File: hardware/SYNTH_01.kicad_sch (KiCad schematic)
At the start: 55 parts, among them J2 Conn_01x04_Pin, SW1 SW_Push_45deg, SW10 SW_Push_45deg, SW11 SW_Push_45deg, SW12 SW_Push_45deg, SW13 SW_Push_45deg, SW14 SW_Push_45deg, SW15 SW_Push_45deg, SW16 SW_Push_45deg, SW17 SW_Push_45deg, SW18 SW_Push_45deg, SW19 SW_Push_45deg, SW2 SW_Push_45deg, SW20 SW_Push_45deg, SW21 SW_Push_45deg, SW3 SW_Push_45deg, SW4 SW_Push_45deg, SW5 SW_Push_45deg, SW6 SW_Push_45deg, SW7 SW_Push_45deg, SW8 SW_Push_45deg, SW9 SW_Push_45deg, U1 MCP23017-E/SP

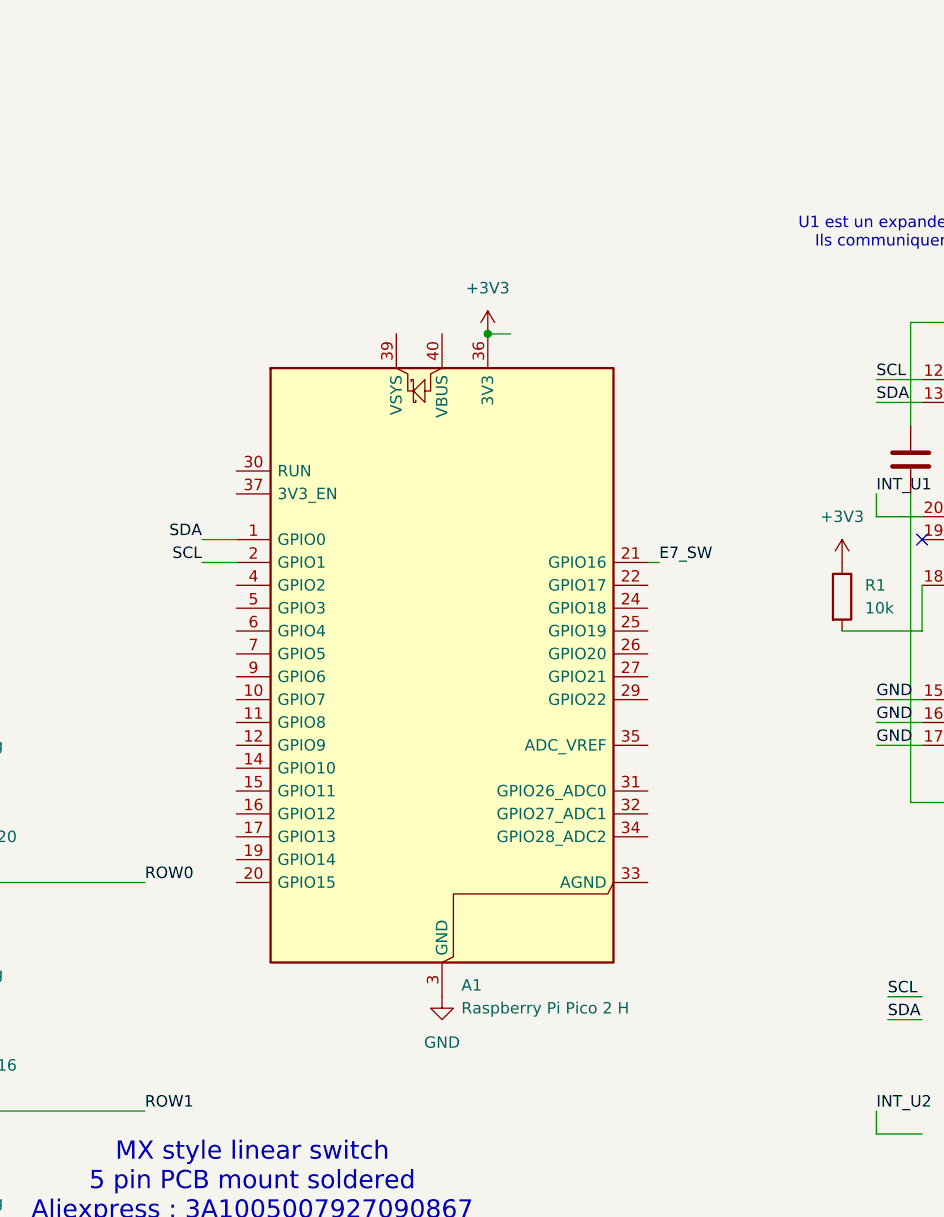
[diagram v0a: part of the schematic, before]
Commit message: PCB: rotary connexion to pico 2
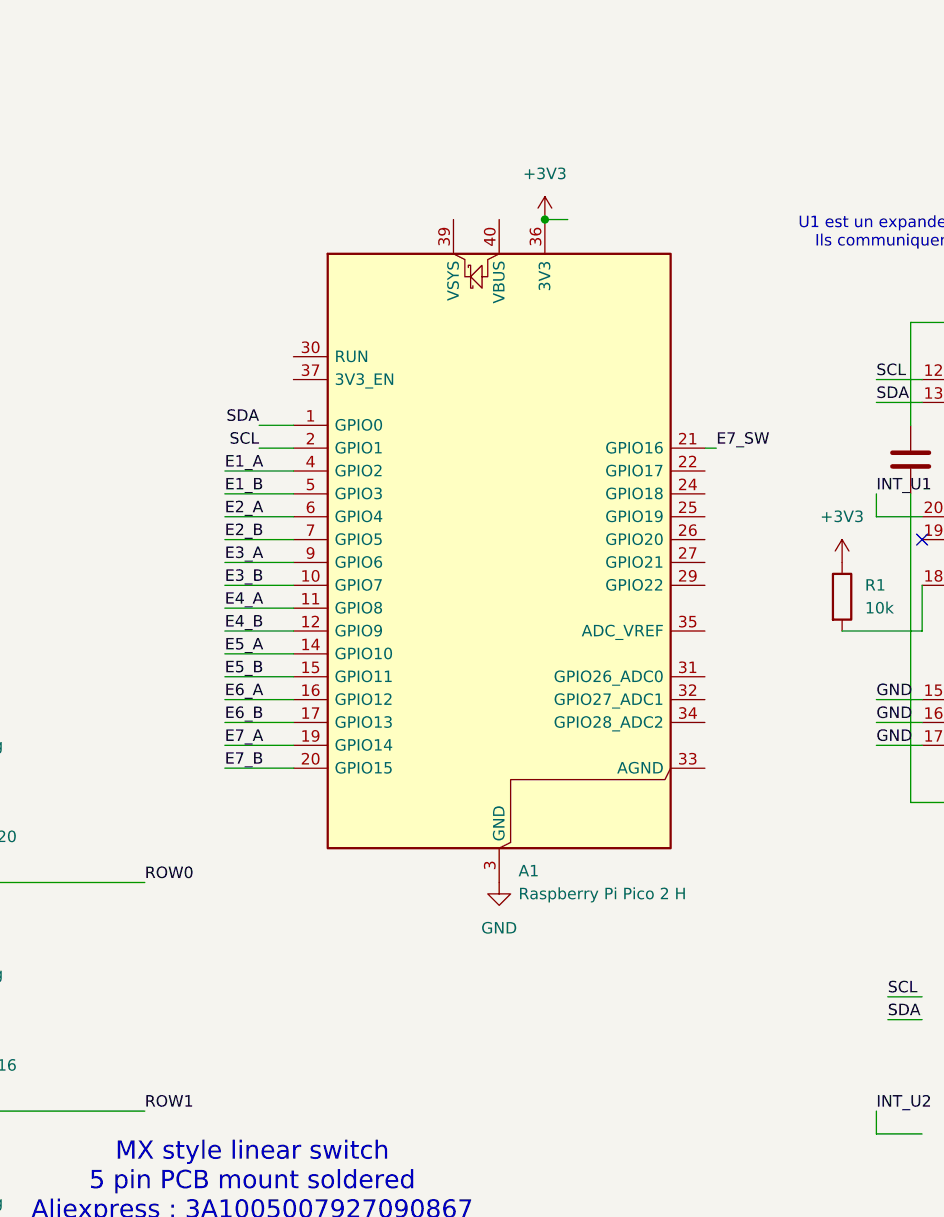
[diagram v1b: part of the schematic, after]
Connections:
- net E1_A: now also A1.4 (GPIO2)
- net E1_B: now also A1.5 (GPIO3)
- net E2_A: now also A1.6 (GPIO4)
- net E2_B: now also A1.7 (GPIO5)
- net E3_A: now also A1.9 (GPIO6)
- net E3_B: now also A1.10 (GPIO7)
- net E4_A: now also A1.11 (GPIO8)
- net E4_B: now also A1.12 (GPIO9)
- net E5_A: now also A1.14 (GPIO10)
- net E5_B: now also A1.15 (GPIO11)
- net E6_A: now also A1.16 (GPIO12)
- net E6_B: now also A1.17 (GPIO13)
- net E7_A: now also A1.19 (GPIO14)
- net E7_B: now also A1.20 (GPIO15)
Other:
- moved on the sheet: A1

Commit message: PCB: adding no connexion markers
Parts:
- D1, D10, D11, D12, D13, D14, D15, D16, D17, D18, D19, D2, D20, D3, D4, D5, D6, D7, D8, D9: value D -> 1N4148
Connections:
- net INT_U1: no longer names the net of U1.20 (INTA)
- no-connect marks 1 -> 17

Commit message: fixing typo in C3 value
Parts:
- C3: value 100nf -> 100nF
- D21: value D -> 1N4148
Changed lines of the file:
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@@
 			)
 		)
-		(property "Value" "100nf"
+		(property "Value" "100nF"
 			(at 99.06 35.5599 0)
 			(show_name no)
@@
 			)
 		)
-		(property "Value" "D"
+		(property "Value" "1N4148"
 			(at 45.72 193.0399 90)
 			(show_name no)

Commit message: PCB: assigning socket to U1 (MCP23017) so the component is replacable is case of break
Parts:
- U1: footprint Package_DIP:DIP-28_W7.62mm -> Package_DIP:DIP-28_W7.62mm_Socket
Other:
- title: SYNTH_01_SCH -> AKOR_01_SCH
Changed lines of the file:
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@@
 	(paper "A4")
 	(title_block
-		(title "SYNTH_01_SCH")
+		(title "AKOR_01_SCH")
 		(date "2026-07-29")
 		(company "Kowskii")
@@
 			)
 		)
-		(property "Footprint" "Package_DIP:DIP-28_W7.62mm"
+		(property "Footprint" "Package_DIP:DIP-28_W7.62mm_Socket"
 			(at 260.35 83.82 0)
 			(hide yes)

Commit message: PCB: assignign footprints to diodes
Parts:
- D1, D10, D11, D12, D13, D14, D15, D16, D17, D18, D19, D2, D20, D21, D3, D4, D5, D6, D7, D8, D9: footprint (none) -> Diode_THT:D_DO-35_SOD27_P10.16mm_Horizontal
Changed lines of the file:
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@@
 			)
 		)
-		(property "Footprint" ""
+		(property "Footprint" "Diode_THT:D_DO-35_SOD27_P10.16mm_Horizontal"
 			(at 59.69 90.17 0)
 			(hide yes)
@@
 			)
 		)
-		(property "Footprint" ""
+		(property "Footprint" "Diode_THT:D_DO-35_SOD27_P10.16mm_Horizontal"
 			(at 135.89 90.17 0)
 			(hide yes)
@@
 			)
 		)
-		(property "Footprint" ""
+		(property "Footprint" "Diode_THT:D_DO-35_SOD27_P10.16mm_Horizontal"
 			(at 59.69 166.37 0)
 			(hide yes)
@@
 			)
 		)
-		(property "Footprint" ""
+		(property "Footprint" "Diode_THT:D_DO-35_SOD27_P10.16mm_Horizontal"
 			(at 110.49 90.17 0)
 			(hide yes)
@@
 			)
 		)
-		(property "Footprint" ""
+		(property "Footprint" "Diode_THT:D_DO-35_SOD27_P10.16mm_Horizontal"
 			(at 59.69 191.77 0)
 			(hide yes)
@@
 			)
 		)
-		(property "Footprint" ""
+		(property "Footprint" "Diode_THT:D_DO-35_SOD27_P10.16mm_Horizontal"
 			(at 110.49 166.37 0)
 			(hide yes)
@@
 			)
 		)
-		(property "Footprint" ""
+		(property "Footprint" "Diode_THT:D_DO-35_SOD27_P10.16mm_Horizontal"
 			(at 110.49 140.97 0)
 			(hide yes)
@@
 			)
 		)
-		(property "Footprint" ""
+		(property "Footprint" "Diode_THT:D_DO-35_SOD27_P10.16mm_Horizontal"
 			(at 85.09 140.97 0)
 			(hide yes)
@@
 			)
 		)
-		(property "Footprint" ""
+		(property "Footprint" "Diode_THT:D_DO-35_SOD27_P10.16mm_Horizontal"
 			(at 59.69 140.97 0)
 			(hide yes)
@@
 			)
 		)
-		(property "Footprint" ""
+		(property "Footprint" "Diode_THT:D_DO-35_SOD27_P10.16mm_Horizontal"
 			(at 85.09 90.17 0)
 			(hide yes)
@@
 			)
 		)
-		(property "Footprint" ""
+		(property "Footprint" "Diode_THT:D_DO-35_SOD27_P10.16mm_Horizontal"
 			(at 85.09 191.77 0)
 			(hide yes)
@@
 			)
 		)
-		(property "Footprint" ""
+		(property "Footprint" "Diode_THT:D_DO-35_SOD27_P10.16mm_Horizontal"
 			(at 135.89 140.97 0)
 			(hide yes)
@@
 			)
 		)
-		(property "Footprint" ""
+		(property "Footprint" "Diode_THT:D_DO-35_SOD27_P10.16mm_Horizontal"
 			(at 85.09 115.57 0)
 			(hide yes)
@@
 			)
 		)
-		(property "Footprint" ""
+		(property "Footprint" "Diode_THT:D_DO-35_SOD27_P10.16mm_Horizontal"
 			(at 43.18 191.77 0)
 			(hide yes)
@@
 			)
 		)
-		(property "Footprint" ""
+		(property "Footprint" "Diode_THT:D_DO-35_SOD27_P10.16mm_Horizontal"
 			(at 85.09 166.37 0)
 			(hide yes)
@@
 			)
 		)
-		(property "Footprint" ""
+		(property "Footprint" "Diode_THT:D_DO-35_SOD27_P10.16mm_Horizontal"
 			(at 135.89 191.77 0)
 			(hide yes)
@@
 			)
 		)
-		(property "Footprint" ""
+		(property "Footprint" "Diode_THT:D_DO-35_SOD27_P10.16mm_Horizontal"
 			(at 110.49 115.57 0)
 			(hide yes)
@@
 			)
 		)
-		(property "Footprint" ""
+		(property "Footprint" "Diode_THT:D_DO-35_SOD27_P10.16mm_Horizontal"
 			(at 135.89 166.37 0)
 			(hide yes)
@@
 			)
 		)
-		(property "Footprint" ""
+		(property "Footprint" "Diode_THT:D_DO-35_SOD27_P10.16mm_Horizontal"
 			(at 110.49 191.77 0)
 			(hide yes)
@@
 			)
 		)
-		(property "Footprint" ""
+		(property "Footprint" "Diode_THT:D_DO-35_SOD27_P10.16mm_Horizontal"
 			(at 59.69 115.57 0)
 			(hide yes)
@@
 			)
 		)
-		(property "Footprint" ""
+		(property "Footprint" "Diode_THT:D_DO-35_SOD27_P10.16mm_Horizontal"
 			(at 135.89 115.57 0)
 			(hide yes)

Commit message: PCB: assign R1 resistor footprint
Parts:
- R1: footprint (none) -> Resistor_THT:R_Axial_DIN0207_L6.3mm_D2.5mm_P10.16mm_Horizontal
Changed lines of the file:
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@@
 			)
 		)
-		(property "Footprint" ""
+		(property "Footprint" "Resistor_THT:R_Axial_DIN0207_L6.3mm_D2.5mm_P10.16mm_Horizontal"
 			(at 231.902 62.23 90)
 			(hide yes)

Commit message: PCB: assign provisional MX switch footprints
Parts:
- SW1, SW10, SW11, SW12, SW13, SW14, SW15, SW16, SW17, SW18, SW19, SW2, SW20, SW21, SW3, SW4, SW5, SW6, SW7, SW8, SW9: footprint (none) -> Button_Switch_Keyboard:SW_Cherry_MX_1.00u_PCB
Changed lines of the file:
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@@
 			)
 		)
-		(property "Footprint" ""
+		(property "Footprint" "Button_Switch_Keyboard:SW_Cherry_MX_1.00u_PCB"
 			(at 107.95 185.42 0)
 			(hide yes)
@@
 			)
 		)
-		(property "Footprint" ""
+		(property "Footprint" "Button_Switch_Keyboard:SW_Cherry_MX_1.00u_PCB"
 			(at 57.15 185.42 0)
 			(hide yes)
@@
 			)
 		)
-		(property "Footprint" ""
+		(property "Footprint" "Button_Switch_Keyboard:SW_Cherry_MX_1.00u_PCB"
 			(at 82.55 185.42 0)
 			(hide yes)
@@
 			)
 		)
-		(property "Footprint" ""
+		(property "Footprint" "Button_Switch_Keyboard:SW_Cherry_MX_1.00u_PCB"
 			(at 57.15 109.22 0)
 			(hide yes)
@@
 			)
 		)
-		(property "Footprint" ""
+		(property "Footprint" "Button_Switch_Keyboard:SW_Cherry_MX_1.00u_PCB"
 			(at 107.95 134.62 0)
 			(hide yes)
@@
 			)
 		)
-		(property "Footprint" ""
+		(property "Footprint" "Button_Switch_Keyboard:SW_Cherry_MX_1.00u_PCB"
 			(at 107.95 83.82 0)
 			(hide yes)
@@
 			)
 		)
-		(property "Footprint" ""
+		(property "Footprint" "Button_Switch_Keyboard:SW_Cherry_MX_1.00u_PCB"
 			(at 133.35 185.42 0)
 			(hide yes)
@@
 			)
 		)
-		(property "Footprint" ""
+		(property "Footprint" "Button_Switch_Keyboard:SW_Cherry_MX_1.00u_PCB"
 			(at 82.55 109.22 0)
 			(hide yes)
@@
 			)
 		)
-		(property "Footprint" ""
+		(property "Footprint" "Button_Switch_Keyboard:SW_Cherry_MX_1.00u_PCB"
 			(at 82.55 134.62 0)
 			(hide yes)
@@
 			)
 		)
-		(property "Footprint" ""
+		(property "Footprint" "Button_Switch_Keyboard:SW_Cherry_MX_1.00u_PCB"
 			(at 107.95 160.02 0)
 			(hide yes)
@@
 			)
 		)
-		(property "Footprint" ""
+		(property "Footprint" "Button_Switch_Keyboard:SW_Cherry_MX_1.00u_PCB"
 			(at 133.35 134.62 0)
 			(hide yes)
@@
 			)
 		)
-		(property "Footprint" ""
+		(property "Footprint" "Button_Switch_Keyboard:SW_Cherry_MX_1.00u_PCB"
 			(at 57.15 134.62 0)
 			(hide yes)
@@
 			)
 		)
-		(property "Footprint" ""
+		(property "Footprint" "Button_Switch_Keyboard:SW_Cherry_MX_1.00u_PCB"
 			(at 133.35 160.02 0)
 			(hide yes)
@@
 			)
 		)
-		(property "Footprint" ""
+		(property "Footprint" "Button_Switch_Keyboard:SW_Cherry_MX_1.00u_PCB"
 			(at 133.35 83.82 0)
 			(hide yes)
@@
 			)
 		)
-		(property "Footprint" ""
+		(property "Footprint" "Button_Switch_Keyboard:SW_Cherry_MX_1.00u_PCB"
 			(at 82.55 160.02 0)
 			(hide yes)
@@
 			)
 		)
-		(property "Footprint" ""
+		(property "Footprint" "Button_Switch_Keyboard:SW_Cherry_MX_1.00u_PCB"
 			(at 40.64 185.42 0)
 			(hide yes)
@@
 			)
 		)
-		(property "Footprint" ""
+		(property "Footprint" "Button_Switch_Keyboard:SW_Cherry_MX_1.00u_PCB"
 			(at 57.15 83.82 0)
 			(hide yes)
@@
 			)
 		)
-		(property "Footprint" ""
+		(property "Footprint" "Button_Switch_Keyboard:SW_Cherry_MX_1.00u_PCB"
 			(at 82.55 83.82 0)
 			(hide yes)
@@
 			)
 		)
-		(property "Footprint" ""
+		(property "Footprint" "Button_Switch_Keyboard:SW_Cherry_MX_1.00u_PCB"
 			(at 57.15 160.02 0)
 			(hide yes)
@@
 			)
 		)
-		(property "Footprint" ""
+		(property "Footprint" "Button_Switch_Keyboard:SW_Cherry_MX_1.00u_PCB"
 			(at 133.35 109.22 0)
 			(hide yes)
@@
 			)
 		)
-		(property "Footprint" ""
+		(property "Footprint" "Button_Switch_Keyboard:SW_Cherry_MX_1.00u_PCB"
 			(at 107.95 109.22 0)
 			(hide yes)

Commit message: PCB: assign provisional EC11 encoder footprints
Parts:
- ENC1, ENC2, ENC3, ENC4, ENC5, ENC6, ENC7: footprint (none) -> Rotary_Encoder:RotaryEncoder_Alps_EC11E-Switch_Vertical_H20mm
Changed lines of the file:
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@@
 			)
 		)
-		(property "Footprint" ""
+		(property "Footprint" "Rotary_Encoder:RotaryEncoder_Alps_EC11E-Switch_Vertical_H20mm"
 			(at 88.9 50.546 0)
 			(hide yes)
@@
 			)
 		)
-		(property "Footprint" ""
+		(property "Footprint" "Rotary_Encoder:RotaryEncoder_Alps_EC11E-Switch_Vertical_H20mm"
 			(at 62.23 50.546 0)
 			(hide yes)
@@
 			)
 		)
-		(property "Footprint" ""
+		(property "Footprint" "Rotary_Encoder:RotaryEncoder_Alps_EC11E-Switch_Vertical_H20mm"
 			(at 34.29 88.646 0)
 			(hide yes)
@@
 			)
 		)
-		(property "Footprint" ""
+		(property "Footprint" "Rotary_Encoder:RotaryEncoder_Alps_EC11E-Switch_Vertical_H20mm"
 			(at 34.29 148.336 0)
 			(hide yes)
@@
 			)
 		)
-		(property "Footprint" ""
+		(property "Footprint" "Rotary_Encoder:RotaryEncoder_Alps_EC11E-Switch_Vertical_H20mm"
 			(at 34.29 117.856 0)
 			(hide yes)
@@
 			)
 		)
-		(property "Footprint" ""
+		(property "Footprint" "Rotary_Encoder:RotaryEncoder_Alps_EC11E-Switch_Vertical_H20mm"
 			(at 34.29 50.546 0)
 			(hide yes)
@@
 			)
 		)
-		(property "Footprint" ""
+		(property "Footprint" "Rotary_Encoder:RotaryEncoder_Alps_EC11E-Switch_Vertical_H20mm"
 			(at 115.57 50.546 0)
 			(hide yes)
